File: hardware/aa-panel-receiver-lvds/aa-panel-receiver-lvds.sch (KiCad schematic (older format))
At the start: 95 parts, among them CN101 Conn_01x02, CN102 Conn_01x02, CN201 8P8C, CN202 Conn_01x08, CN251 Conn_01x08, CN301 8P8C, CN302 Conn_01x08, CN351 Conn_01x08, U101 CRE1S0505S3C, U201 ST26C32, U202 Si8640EB-B-IU, U301 ST26C32, U302 Si8640EB-B-IU

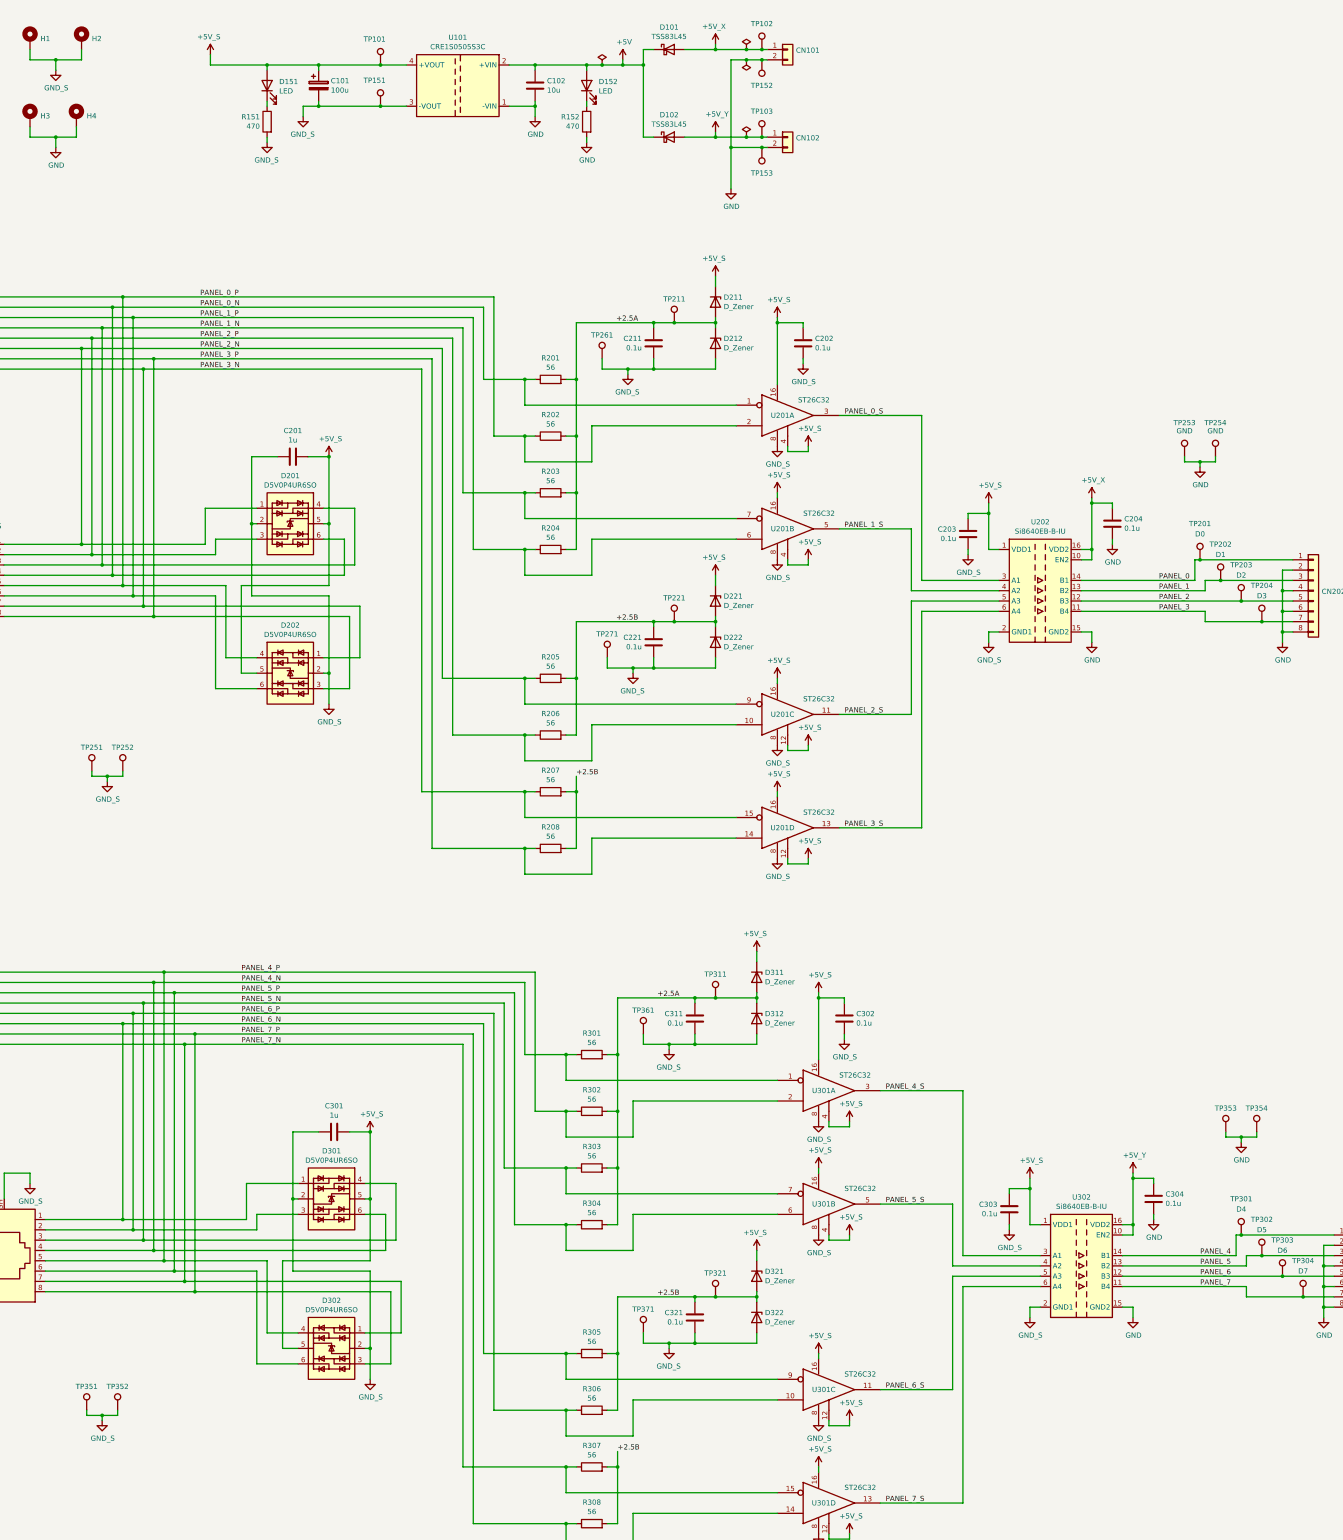
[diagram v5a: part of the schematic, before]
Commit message: Placement of components on panel receiver board, routing TBD
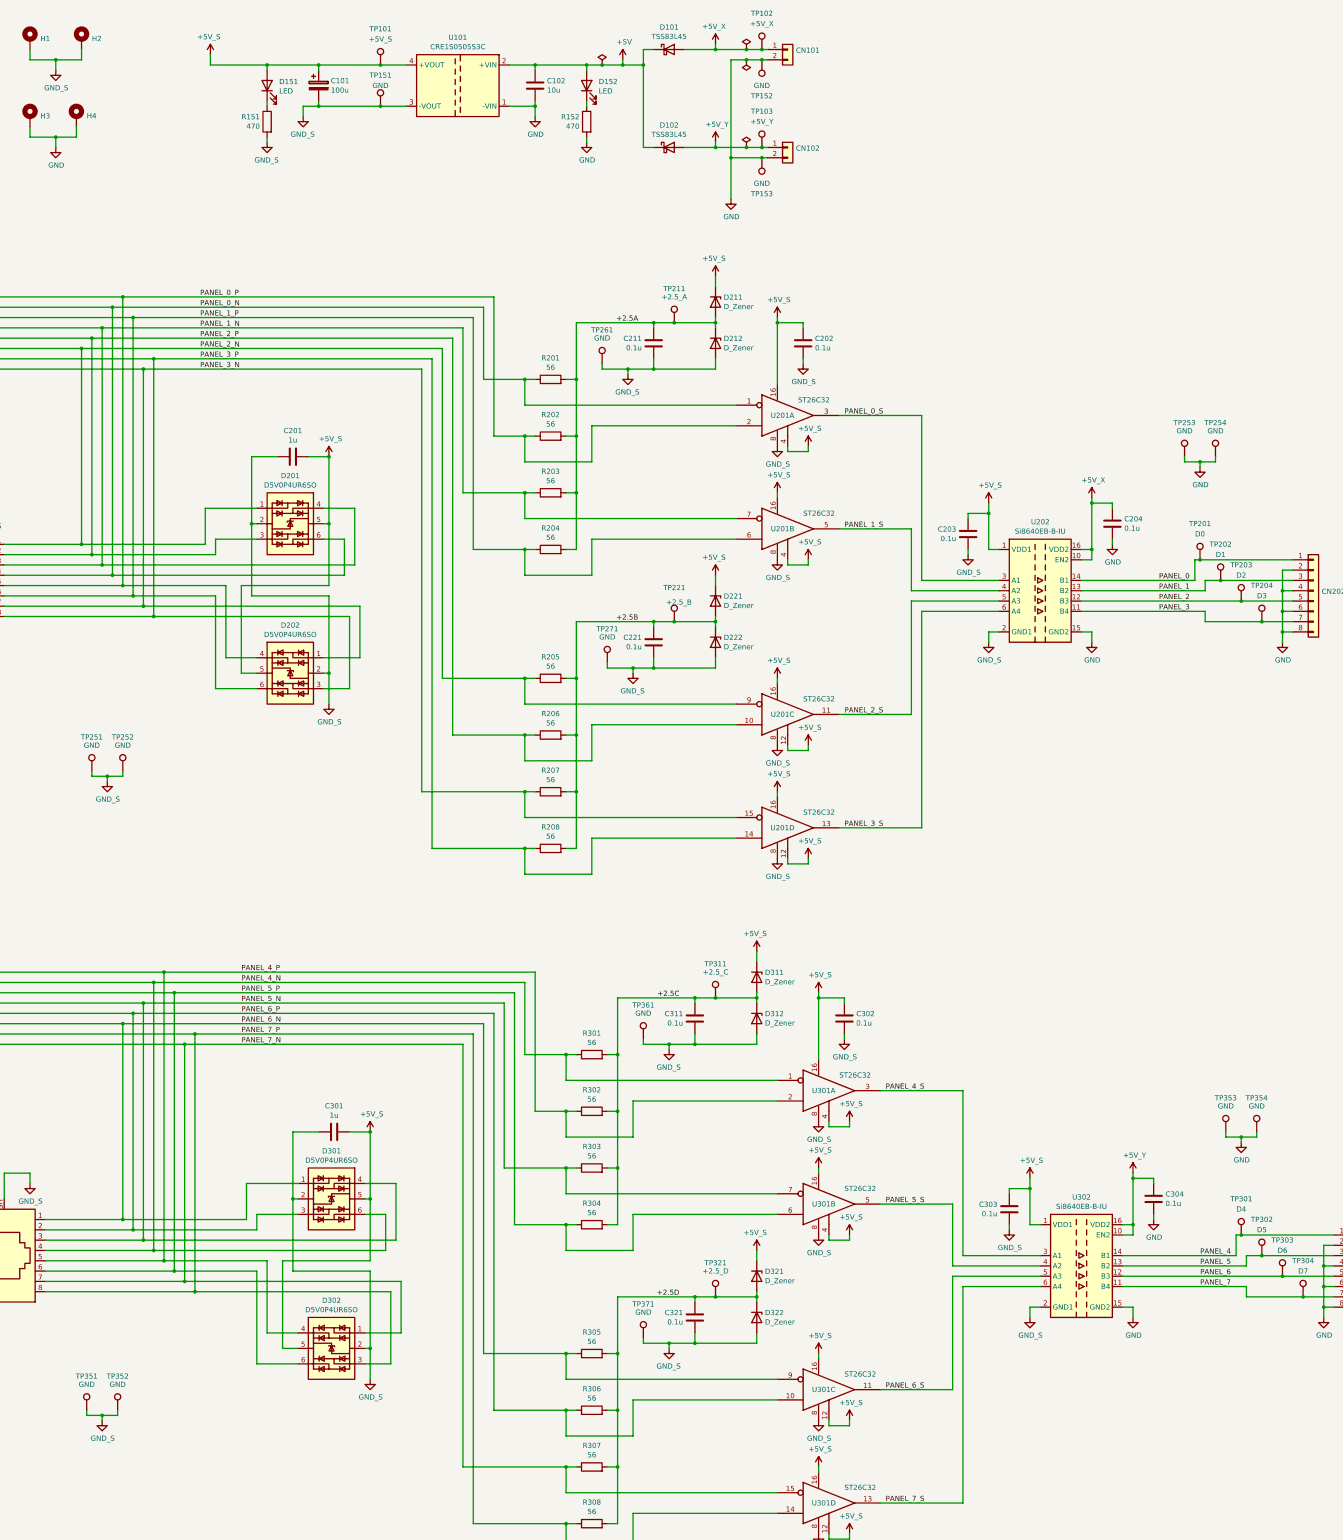
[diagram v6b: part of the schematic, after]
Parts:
- TP101: value TestPoint -> +5V_S
- TP102: value TestPoint -> +5V_X
- TP103: value TestPoint -> +5V_Y
- TP151, TP152, TP153, TP251, TP252, TP261, TP271, TP351, TP352, TP353, TP354, TP361, TP371: value TestPoint -> GND
- TP211: value TestPoint -> +2.5_A
- TP221: value TestPoint -> +2.5_B
- TP311: value TestPoint -> +2.5_C
- TP321: value TestPoint -> +2.5_D
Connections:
- net +2.5A: no longer C311.1, D311.2 (A), D312.1 (K), R301.2, R302.2, R303.2, R304.2, TP311.1
- net +2.5B: no longer C321.1, D321.2 (A), D322.1 (K), R305.2, R306.2, R307.2, R308.2, TP321.1
- new net +2.5C: C311.1, D311.2 (A), D312.1 (K), R301.2, R302.2, R303.2, R304.2, TP311.1
- new net +2.5D: C321.1, D321.2 (A), D322.1 (K), R305.2, R306.2, R307.2, R308.2, TP321.1
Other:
- moved on the sheet: CN102, D102, TP103, TP153, TP261, TP271, TP361, TP371

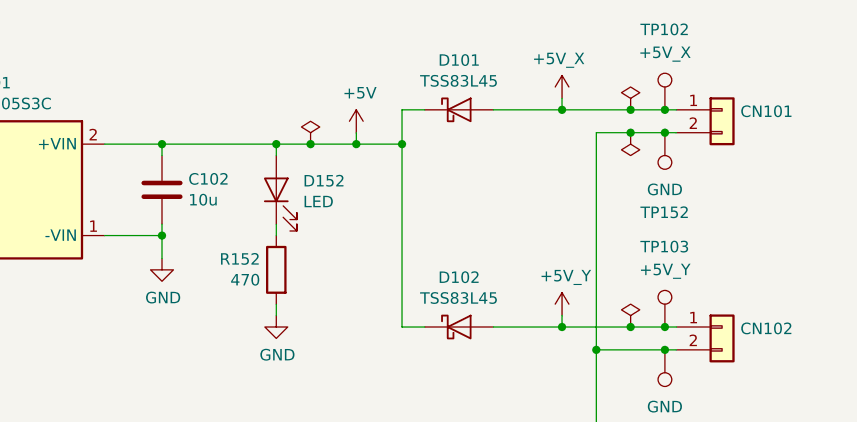
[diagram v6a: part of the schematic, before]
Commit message: Second rount almost ready, less fiducials
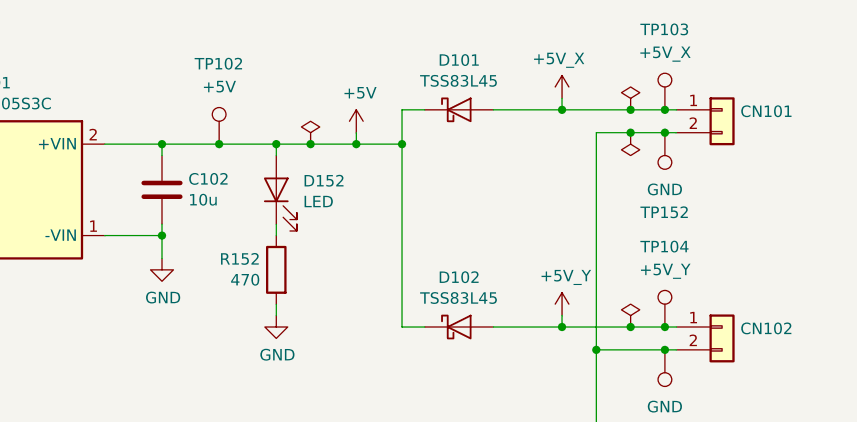
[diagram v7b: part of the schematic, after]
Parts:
- added TP102: +5V, aa-shared:TestPoint_Loop_D1.80mm_Drill1.0mm_Beaded, symbol Connector:TestPoint
- renumbered TP102 to TP103, TP103 to TP104
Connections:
- net +5V: now also TP102.1
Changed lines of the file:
@@
 	10350 4750 10250 4750
 $Comp
-L Connector:TestPoint TP103
+L Connector:TestPoint TP104
 U 1 1 5DDFDC67
 P 12150 1950
-F 0 "TP103" H 12150 2300 50  0000 C CNN
+F 0 "TP104" H 12150 2300 50  0000 C CNN
 F 1 "+5V_Y" H 12150 2200 50  0000 C CNN
 F 2 "aa-shared:TestPoint_Loop_D1.80mm_Drill1.0mm_Beaded" H 12350 1950 50  0001 C CNN
@@
 	10450 1150 10450 1200
 Wire Wire Line
-	10450 1150 9950 1150
+	10450 1150 10200 1150
 $Comp
 L power:GND #PWR020
@@
 $EndComp
 $Comp
-L Connector:TestPoint TP102
+L Connector:TestPoint TP103
 U 1 1 5E3A63F4
 P 12150 1000
-F 0 "TP102" H 12150 1350 50  0000 C CNN
+F 0 "TP103" H 12150 1350 50  0000 C CNN
 F 1 "+5V_X" H 12150 1250 50  0000 C CNN
 F 2 "aa-shared:TestPoint_Loop_D1.80mm_Drill1.0mm_Beaded" H 12350 1000 50  0001 C CNN
@@
 	10350 7650 10350 8200
 Connection ~ 10350 7650
+$Comp
+L Connector:TestPoint TP102
+U 1 1 5D0CCED8
+P 10200 1150
+F 0 "TP102" H 10200 1500 50  0000 C CNN
+F 1 "+5V" H 10200 1400 50  0000 C CNN
+F 2 "aa-shared:TestPoint_Loop_D1.80mm_Drill1.0mm_Beaded" H 10400 1150 50  0001 C CNN
+F 3 "" H 10400 1150 50  0001 C CNN
+	1    10200 1150
+	-1   0    0    -1
+$EndComp
+Connection ~ 10200 1150
+Wire Wire Line
+	10200 1150 9950 1150
 $EndSCHEMATC

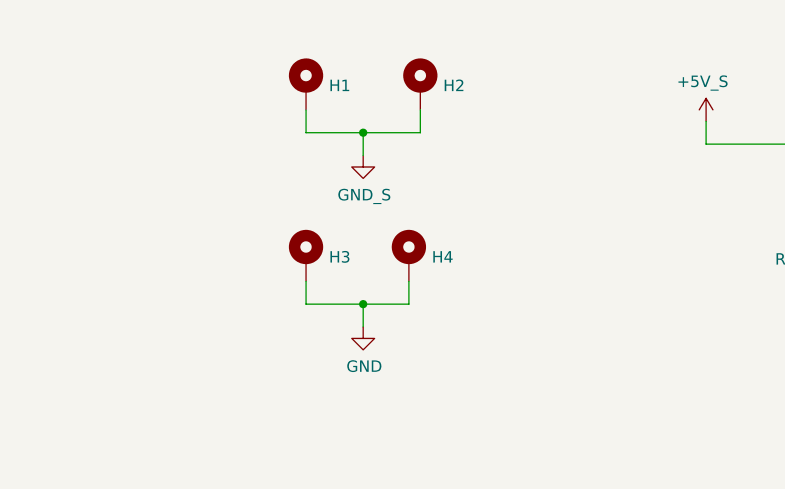
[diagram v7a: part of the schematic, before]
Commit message: Final designs and actual sent gerbers for first for-real run
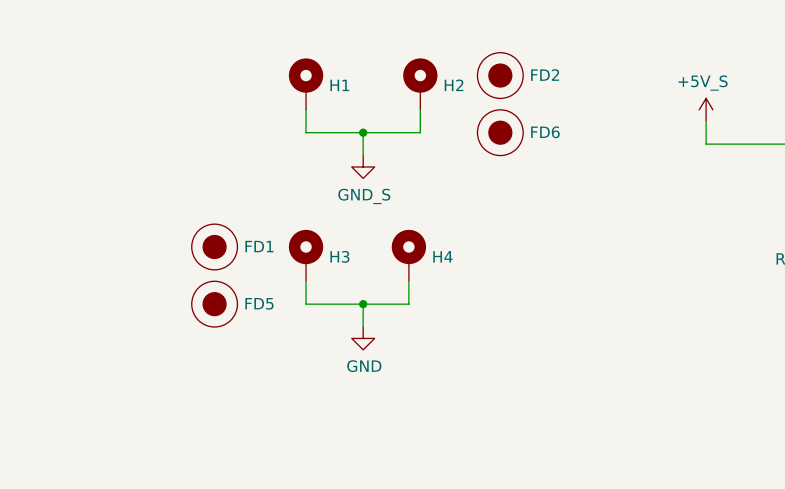
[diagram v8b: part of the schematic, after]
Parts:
- added FD1, FD2: Fiducial, Fiducial:Fiducial_1mm_Dia_2.54mm_Outer_CopperTop, symbol aa-shared:Fiducial
- added FD5, FD6: Fiducial, aa-shared:StencilAlignment_1.27mm, symbol aa-shared:Fiducial
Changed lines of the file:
@@
 Wire Wire Line
 	10200 1150 9950 1150
+$Comp
+L aa-shared:Fiducial FD1
+U 1 1 5D147B17
+P 4650 1600
+F 0 "FD1" H 4778 1600 50  0000 L CNN
+F 1 "Fiducial" H 4650 1750 50  0001 C CNN
+F 2 "Fiducial:Fiducial_1mm_Dia_2.54mm_Outer_CopperTop" H 4650 1600 50  0001 C CNN
+F 3 "" H 4650 1600 50  0001 C CNN
+	1    4650 1600
+	1    0    0    -1
+$EndComp
+$Comp
+L aa-shared:Fiducial FD2
+U 1 1 5D147E31
+P 5900 850
+F 0 "FD2" H 6028 850 50  0000 L CNN
+F 1 "Fiducial" H 5900 1000 50  0001 C CNN
+F 2 "Fiducial:Fiducial_1mm_Dia_2.54mm_Outer_CopperTop" H 5900 850 50  0001 C CNN
+F 3 "" H 5900 850 50  0001 C CNN
+	1    5900 850
+	1    0    0    -1
+$EndComp
+$Comp
+L aa-shared:Fiducial FD5
+U 1 1 5D147FBF
+P 4650 1850
+F 0 "FD5" H 4778 1850 50  0000 L CNN
+F 1 "Fiducial" H 4650 2000 50  0001 C CNN
+F 2 "aa-shared:StencilAlignment_1.27mm" H 4650 1850 50  0001 C CNN
+F 3 "" H 4650 1850 50  0001 C CNN
+	1    4650 1850
+	1    0    0    -1
+$EndComp
+$Comp
+L aa-shared:Fiducial FD6
+U 1 1 5D148209
+P 5900 1100
+F 0 "FD6" H 6028 1100 50  0000 L CNN
+F 1 "Fiducial" H 5900 1250 50  0001 C CNN
+F 2 "aa-shared:StencilAlignment_1.27mm" H 5900 1100 50  0001 C CNN
+F 3 "" H 5900 1100 50  0001 C CNN
+	1    5900 1100
+	1    0    0    -1
+$EndComp
 $EndSCHEMATC
